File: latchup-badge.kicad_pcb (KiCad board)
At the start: 2 copper layers, 85.7 x 54 mm, 55 parts, among them J1 USB_C_Receptacle_USB2.0, J2 Connector_Generic:Conn_02x06_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, J3 Connector_Generic:Conn_02x06_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, J4 Connector_Generic:Conn_02x05_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, J5 Connector_Generic:Conn_02x06_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, SW1 SW_Push, SW2 SW_Push, U1 ICE40UP5K-SG48ITR, U2 TLV70012_SOT23-5, U3 TLV70033_SOT23-5, U4 M25PX32-VMW, U5 LY68L6400, X1 ASE-12.000MHz

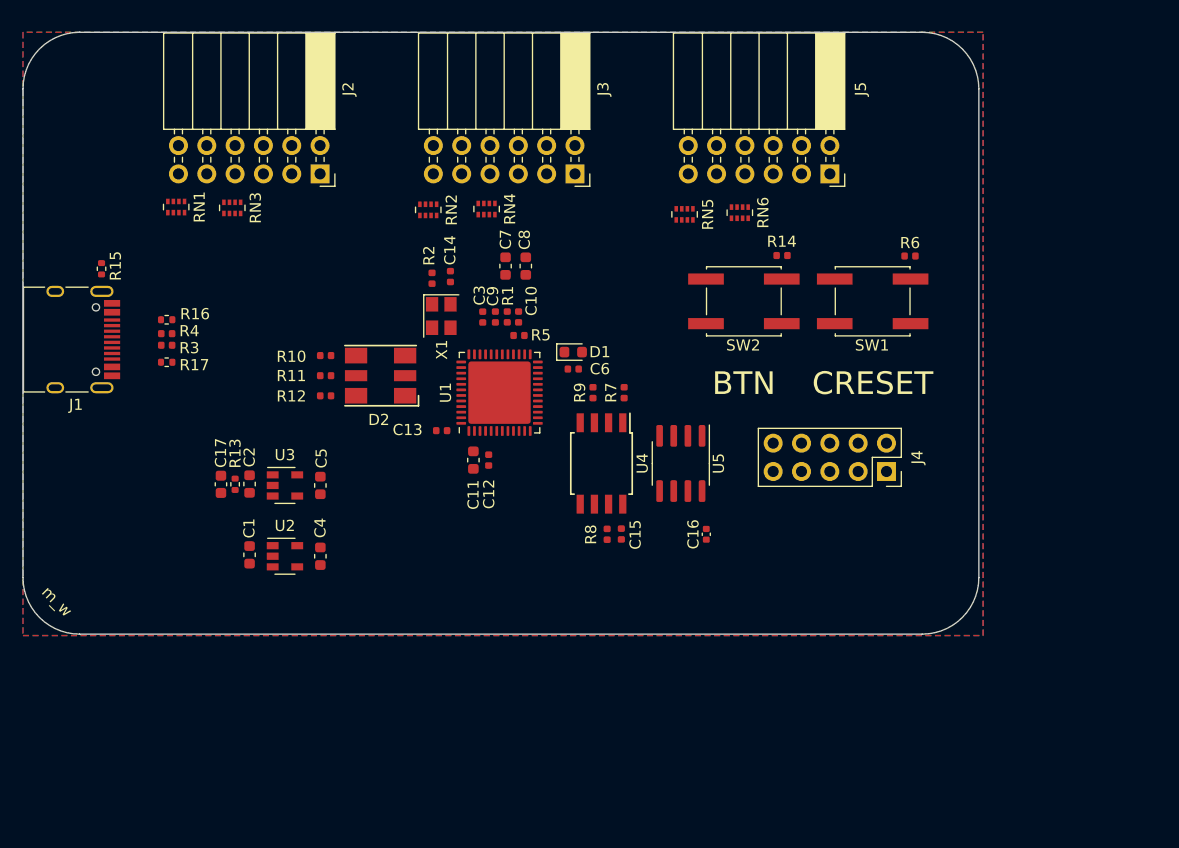
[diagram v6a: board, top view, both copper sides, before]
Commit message: Routed board
Switched to 4 layer design and routed it.

Signed-off-by: Michael Welling <mwelling@ieee.org>
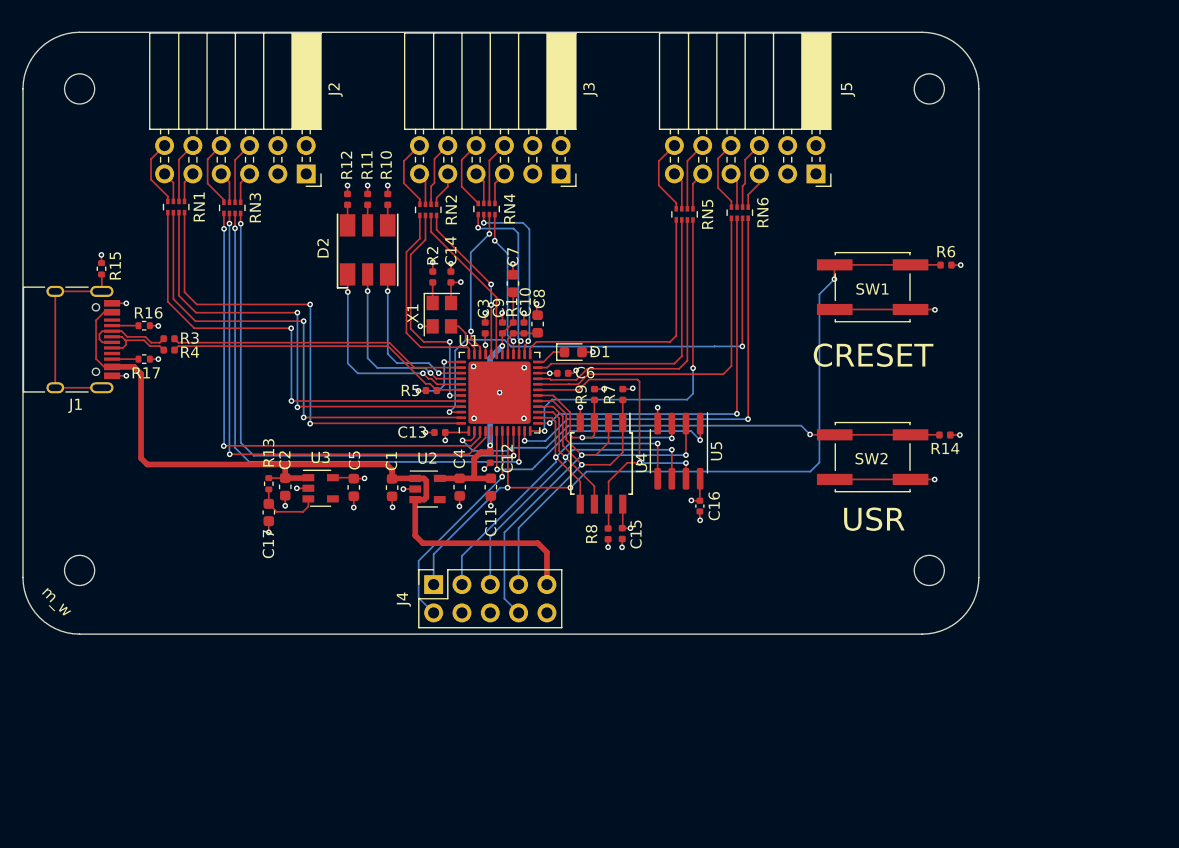
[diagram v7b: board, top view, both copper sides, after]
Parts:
- added REF**: MountingHole_2.7mm_M2.5, MountingHole:MountingHole_2.7mm_M2.5, F.Cu at (81.3, 55.9)
- added REF**: MountingHole_2.7mm_M2.5, MountingHole:MountingHole_2.7mm_M2.5, F.Cu at (157.5, 55.9)
- added REF**: MountingHole_2.7mm_M2.5, MountingHole:MountingHole_2.7mm_M2.5, F.Cu at (81.3, 99.1)
- added REF**: MountingHole_2.7mm_M2.5, MountingHole:MountingHole_2.7mm_M2.5, F.Cu at (157.5, 99.1)
- moved J4 41.9 mm to (113.0, 100.3), turned to 90 degrees
- moved R14 21.7 mm to (158.9, 86.9), turned to 0 degrees
- moved SW2 18.1 mm to (152.4, 88.9)
- moved R12 17.7 mm to (105.3, 65.8), turned to 90 degrees
- moved R11 16.3 mm to (107.1, 65.8), turned to 90 degrees
- moved R10 15.1 mm to (108.9, 65.8), turned to 90 degrees
- moved C1 14.1 mm to (109.3, 91.6)
- moved U2 14.1 mm to (112.5, 91.8)
- moved C4 13.9 mm to (115.4, 91.6)
- moved D2 11.3 mm to (107.1, 70.3), turned to 90 degrees
- moved R5 9.28 mm to (112.8, 82.9)
- moved C8 5.30 mm to (122.4, 77.0)
- moved C17 4.98 mm to (98.2, 93.9), turned to -90 degrees
- moved R6 3.33 mm to (159.0, 71.7)
- moved U3 3.21 mm to (102.9, 91.7)
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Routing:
- net /CRESET: track 0.00 -> 73.6 mm, vias 0 -> 3
- net +5V: track 0.00 -> 69.5 mm
- net /PIN10: track 0.00 -> 49.8 mm, vias 0 -> 2
- net /PIN9: track 0.00 -> 47.7 mm, vias 0 -> 2
- net /BTN_A: track 0.00 -> 46.2 mm, vias 0 -> 2
- net /PIN4: track 0.00 -> 45.8 mm, vias 0 -> 2
- net /PIN3: track 0.00 -> 44.7 mm, vias 0 -> 2
- net /PIN46: track 0.00 -> 44.7 mm, vias 0 -> 2
- net GND: track 0.00 -> 43.9 mm, vias 0 -> 34
- net /PIN48: track 0.00 -> 43.1 mm, vias 0 -> 2
- net /PIN47: track 0.00 -> 43.0 mm, vias 0 -> 2
- net /PIN45: track 0.00 -> 41.9 mm, vias 0 -> 2
- net /PIN44: track 0.00 -> 41.8 mm, vias 0 -> 2
- net /ICE40_SPI_SI: track 0.00 -> 41.7 mm, vias 0 -> 2
- net /PIN11: track 0.00 -> 39.7 mm, vias 0 -> 2
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- added copper zone on In2.Cu, net +3V3
- added copper zone on In1.Cu, net GND
- removed copper zone on B.Cu, net +3V3
- removed copper zone on F.Cu, net GND
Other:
- copper layers 2 -> 4
- board text added: "USR"
- board text removed: "BTN"
